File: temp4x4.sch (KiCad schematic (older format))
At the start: 15 parts, among them J1 NUCLEO_CN6_1-6, J2 NUCLEO_CN5_10-1, U1 LP5907MFX-3.3_NOPB, U2 ADS124S08IPBS

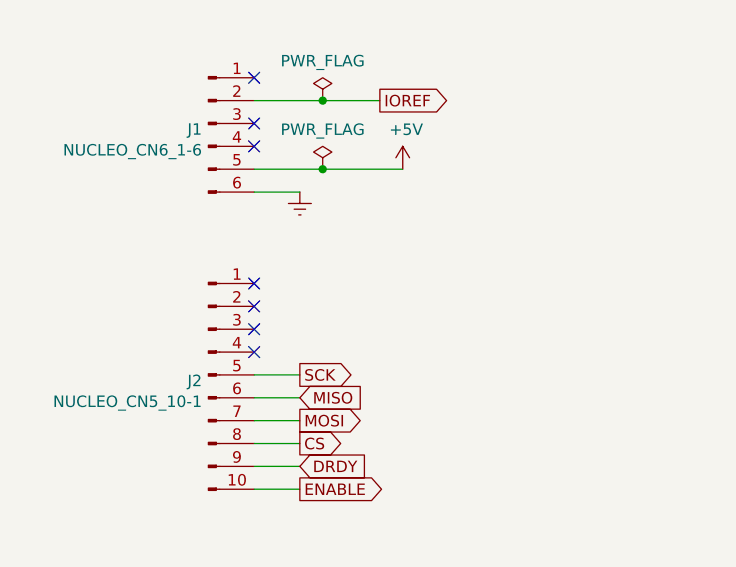
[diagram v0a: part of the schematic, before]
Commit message: added second GND connection through second pin header
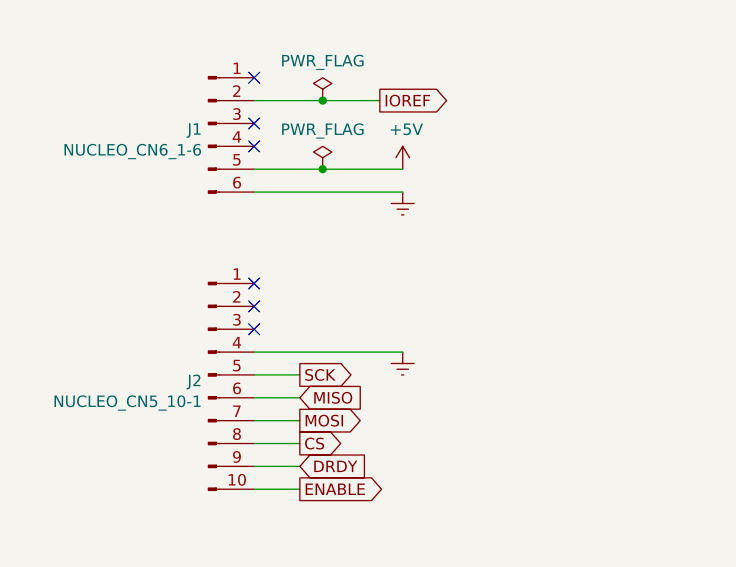
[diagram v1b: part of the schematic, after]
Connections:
- net Earth: now also J2.4 (Pin_4)
- no-connect marks 9 -> 8
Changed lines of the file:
@@
 L power:Earth #PWR03
 U 1 1 5ECDA4EC
-P 1750 3450
-F 0 "#PWR03" H 1750 3200 50  0001 C CNN
-F 1 "Earth" H 1750 3300 50  0001 C CNN
-F 2 "" H 1750 3450 50  0001 C CNN
-F 3 "~" H 1750 3450 50  0001 C CNN
-	1    1750 3450
-	1    0    0    -1
-$EndComp
-Wire Wire Line
-	1550 3450 1750 3450
+P 2200 3450
+F 0 "#PWR03" H 2200 3200 50  0001 C CNN
+F 1 "Earth" H 2200 3300 50  0001 C CNN
+F 2 "" H 2200 3450 50  0001 C CNN
+F 3 "~" H 2200 3450 50  0001 C CNN
+	1    2200 3450
+	1    0    0    -1
+$EndComp
+Wire Wire Line
+	1550 3450 2200 3450
 Wire Wire Line
 	1550 4250 1750 4250
@@
 	1    0    0    -1
 $EndComp
-NoConn ~ 1550 4150
 NoConn ~ 1550 4050
 NoConn ~ 1550 3950
@@
 Wire Wire Line
 	5800 3300 5800 4350
+$Comp
+L power:Earth #PWR?
+U 1 1 5EC59F0A
+P 2200 4150
+F 0 "#PWR?" H 2200 3900 50  0001 C CNN
+F 1 "Earth" H 2200 4000 50  0001 C CNN
+F 2 "" H 2200 4150 50  0001 C CNN
+F 3 "~" H 2200 4150 50  0001 C CNN
+	1    2200 4150
+	1    0    0    -1
+$EndComp
+Wire Wire Line
+	1550 4150 2200 4150
 $EndSCHEMATC

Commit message: completed ground connections
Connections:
- net Earth: no longer J2.4 (Pin_4)
- no-connect marks 8 -> 9
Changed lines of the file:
@@
 Wire Wire Line
 	5800 3300 5800 4350
-$Comp
-L power:Earth #PWR?
-U 1 1 5EC59F0A
-P 2200 4150
-F 0 "#PWR?" H 2200 3900 50  0001 C CNN
-F 1 "Earth" H 2200 4000 50  0001 C CNN
-F 2 "" H 2200 4150 50  0001 C CNN
-F 3 "~" H 2200 4150 50  0001 C CNN
-	1    2200 4150
-	1    0    0    -1
-$EndComp
-Wire Wire Line
-	1550 4150 2200 4150
+NoConn ~ 1550 4150
 $EndSCHEMATC

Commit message: start re-doing the analog part
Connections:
- net RTD_0_1/IEXC: no longer names the net of U2.2 (AIN5)
- net RTD_0_1/REF_N: no longer names the net of U2.29 (REFN0)
- net RTD_0_1/REF_P: no longer names the net of U2.30 (REFP0)
- net RTD_0_1/RTD0_N: no longer names the net of U2.20 (GPIO2_AIN10)
- net RTD_0_1/RTD0_P: no longer names the net of U2.19 (GPIO3_AIN11)
- net RTD_0_1/RTD1_N: no longer names the net of U2.22 (GPIO0_AIN8)
- net RTD_0_1/RTD1_P: no longer names the net of U2.21 (GPIO1_AIN9)
- net RTD_1_2/IEXC: no longer names the net of U2.7 (AIN0)
- net RTD_1_2/REF_N: no longer names the net of U2.31 (REFN1_AIN7)
- net RTD_1_2/REF_P: no longer names the net of U2.32 (REFP1_AIN6)
- net RTD_1_2/RTD0_N: no longer names the net of U2.4 (AIN3)
- net RTD_1_2/RTD0_P: no longer names the net of U2.3 (AIN4)
- net RTD_1_2/RTD1_N: no longer names the net of U2.6 (AIN1)
- net RTD_1_2/RTD1_P: no longer names the net of U2.5 (AIN2)
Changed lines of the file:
@@
 $Descr A4 11693 8268
 encoding utf-8
-Sheet 1 3
+Sheet 1 1
 Title ""
 Date ""
@@
 Text GLabel 6250 1800 2    50   Input ~ 0
 IOREF
-$Sheet
-S 3950 4050 1250 1150
-U 5EC374D6
-F0 "RTD_0_1" 50
-F1 "two_rtd_plus_ref.sch" 50
-F2 "IEXC" I R 5200 4250 50
-F3 "RTD0_P" O R 5200 4400 50
-F4 "RTD0_N" O R 5200 4500 50
-F5 "RTD1_P" O R 5200 4650 50
-F6 "RTD1_N" O R 5200 4750 50
-F7 "REF_P" O R 5200 4900 50
-F8 "REF_N" O R 5200 5000 50
-$EndSheet
 Wire Wire Line
 	6700 4950 6700 5000
@@
 Connection ~ 6700 4950
 NoConn ~ 7000 2650
-$Sheet
-S 3950 2350 1250 1150
-U 5ED0B429
-F0 "RTD_1_2" 50
-F1 "two_rtd_plus_ref.sch" 50
-F2 "IEXC" I R 5200 2550 50
-F3 "RTD0_P" O R 5200 2700 50
-F4 "RTD0_N" O R 5200 2800 50
-F5 "RTD1_P" O R 5200 2950 50
-F6 "RTD1_N" O R 5200 3050 50
-F7 "REF_P" O R 5200 3200 50
-F8 "REF_N" O R 5200 3300 50
-$EndSheet
 $Comp
 L power:Earth #PWR06
@@
 NoConn ~ 1550 3950
 NoConn ~ 1550 3850
-Wire Wire Line
-	5200 3200 5900 3200
-Wire Wire Line
-	5200 3300 5800 3300
-Wire Wire Line
-	5650 4250 5200 4250
-Wire Wire Line
-	6000 4400 5200 4400
-Wire Wire Line
-	6100 4500 5200 4500
-Wire Wire Line
-	6200 4650 5200 4650
-Wire Wire Line
-	6300 4750 5200 4750
-Wire Wire Line
-	6400 4900 5200 4900
-Wire Wire Line
-	6500 5000 5200 5000
-Wire Wire Line
-	6700 2550 6700 2850
-Wire Wire Line
-	6700 2850 7000 2850
-Wire Wire Line
-	5200 2550 6700 2550
-Wire Wire Line
-	5200 2700 6600 2700
-Wire Wire Line
-	5200 2800 6500 2800
-Wire Wire Line
-	7000 3350 5650 3350
-Wire Wire Line
-	5650 3350 5650 4250
 $Comp
 L ADS124S08IPBS:ADS124S08IPBS U2
@@
 	1    0    0    -1
 $EndComp
-Wire Wire Line
-	6600 3250 7000 3250
-Wire Wire Line
-	6600 2700 6600 3250
-Wire Wire Line
-	6500 3150 7000 3150
-Wire Wire Line
-	6500 2800 6500 3150
-Wire Wire Line
-	5200 2950 6000 2950
-Wire Wire Line
-	6400 3050 7000 3050
-Wire Wire Line
-	5200 3050 6300 3050
-Wire Wire Line
-	6300 3050 6300 2950
-Wire Wire Line
-	6300 2950 7000 2950
-Wire Wire Line
-	6000 2950 6000 3150
-Wire Wire Line
-	6000 3150 6400 3150
-Wire Wire Line
-	6400 3150 6400 3050
-Wire Wire Line
-	6200 3650 7000 3650
-Wire Wire Line
-	6200 3650 6200 4650
-Wire Wire Line
-	6300 4750 6300 3550
-Wire Wire Line
-	6300 3550 7000 3550
-Wire Wire Line
-	6000 4400 6000 3850
-Wire Wire Line
-	6000 3850 7000 3850
-Wire Wire Line
-	6100 4500 6100 3750
-Wire Wire Line
-	6100 3750 7000 3750
-Wire Wire Line
-	6400 4050 7000 4050
-Wire Wire Line
-	6400 4050 6400 4900
-Wire Wire Line
-	6500 4150 7000 4150
-Wire Wire Line
-	6500 4150 6500 5000
-Wire Wire Line
-	5900 4250 6850 4250
-Wire Wire Line
-	6850 4250 6850 4350
-Wire Wire Line
-	6850 4350 7000 4350
-Wire Wire Line
-	5900 3200 5900 4250
-Wire Wire Line
-	5800 4350 6750 4350
-Wire Wire Line
-	6750 4350 6750 4450
-Wire Wire Line
-	6750 4450 7000 4450
-Wire Wire Line
-	5800 3300 5800 4350
 NoConn ~ 1550 4150
 $EndSCHEMATC

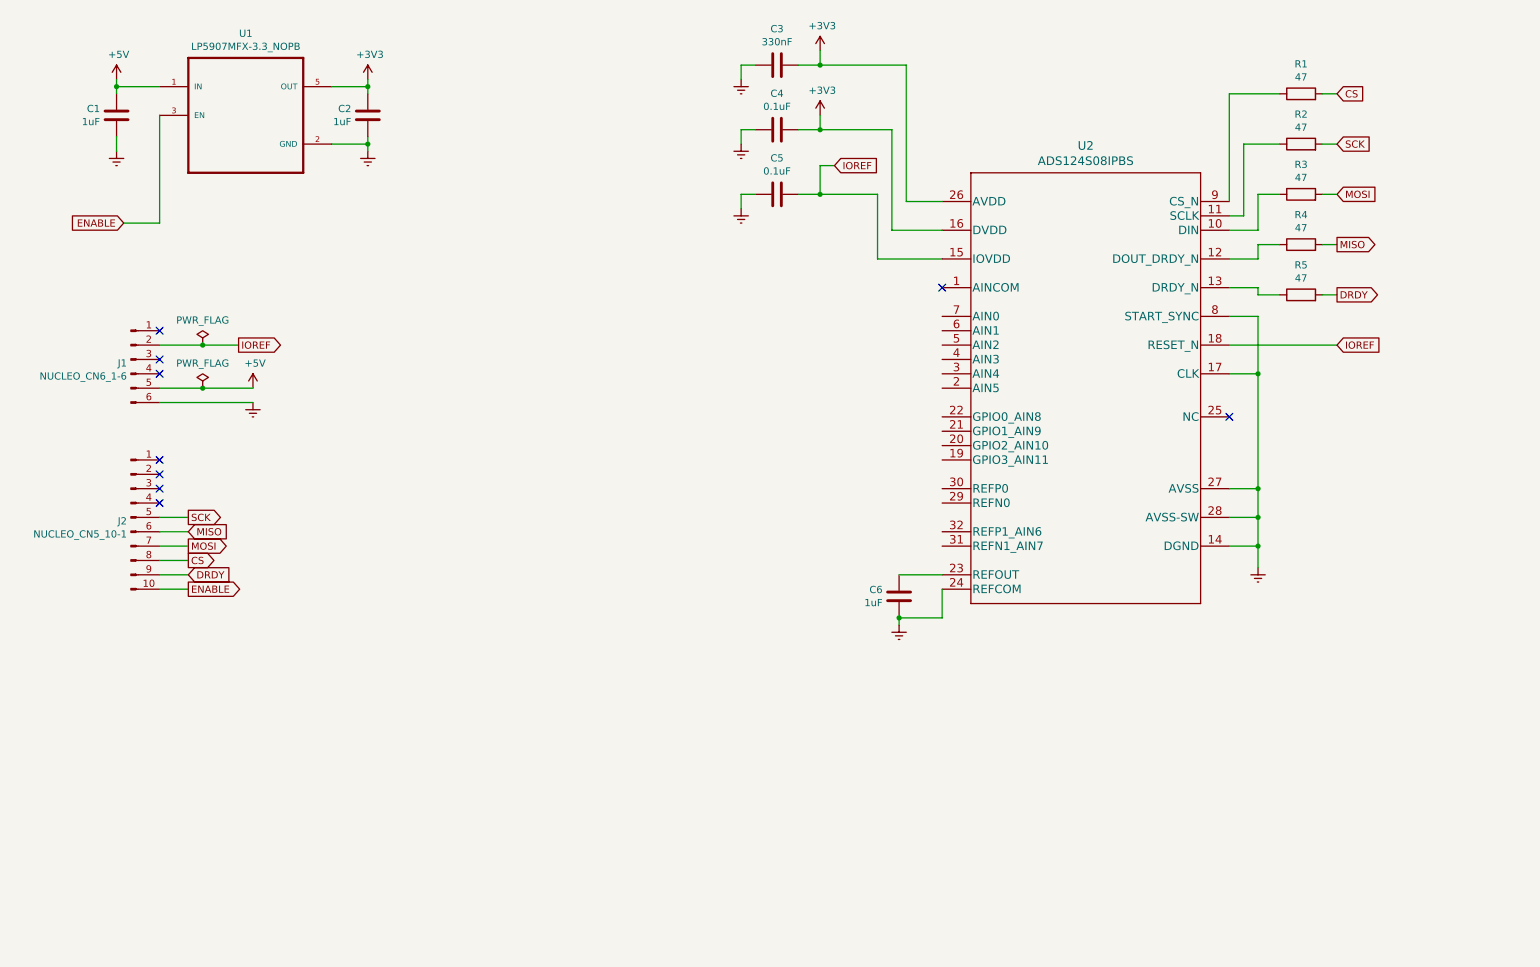
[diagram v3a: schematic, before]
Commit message: re-done analog part of the circuit
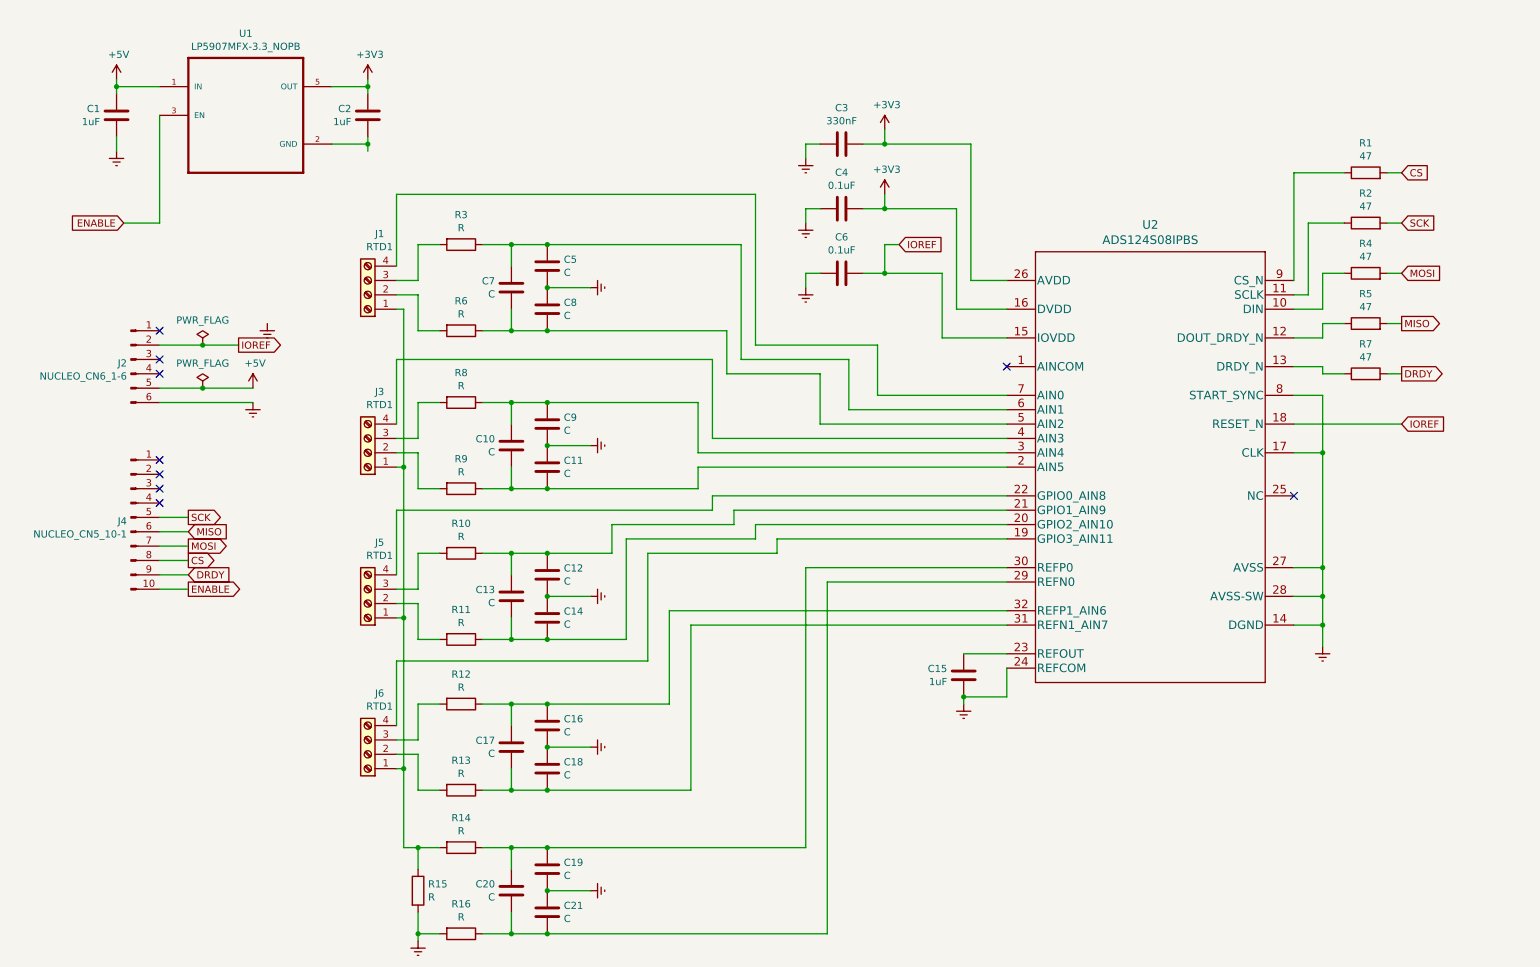
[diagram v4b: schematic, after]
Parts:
- added C10, C11, C12, C13, C14, C16, C17, C18, C19, C20, C21, C5, C7, C8, C9: C, Capacitor_SMD:C_0805_2012Metric_Pad1.15x1.40mm_HandSolder, symbol Device:C
- added J1, J3, J5, J6: RTD1, temp4x4:screw_term_4x, symbol Connector:Screw_Terminal_01x04
- added R10, R11, R12, R13, R14, R15, R16, R3, R6, R8, R9: R, Resistor_SMD:R_0805_2012Metric_Pad1.15x1.40mm_HandSolder, symbol Device:R
- renumbered C6 to C15, C5 to C6, J1 to J2, J2 to J4, R3 to R4, R4 to R5, R5 to R7
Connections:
- net Earth: now also C11.1, C12.2, C14.1, C16.2, C18.1, C19.2, C21.1, C5.2, C8.1, C9.2, R15.2, R16.2; no longer C2.2, U1.2 (GND)
- net at U2.19 (GPIO3_AIN11): now also J6.4 (Pin_4)
- net at U2.2 (AIN5): now also C10.1, C11.2, R9.1
- net at U2.20 (GPIO2_AIN10): now also C13.1, C14.2, R11.1
- net at U2.21 (GPIO1_AIN9): now also C12.1, C13.2, R10.1
- net at U2.22 (GPIO0_AIN8): now also J5.4 (Pin_4)
- net at U2.29 (REFN0): now also C20.1, C21.2, R16.1
- net at U2.3 (AIN4): now also C10.2, C9.1, R8.1
- net at U2.30 (REFP0): now also C19.1, C20.2, R14.1
- net at U2.31 (REFN1_AIN7): now also C17.1, C18.2, R13.1
- net at U2.32 (REFP1_AIN6): now also C16.1, C17.2, R12.1
- net at U2.4 (AIN3): now also J3.4 (Pin_4)
- net at U2.5 (AIN2): now also C7.1, C8.2, R6.1
- net at U2.6 (AIN1): now also C5.1, C7.2, R3.1
- net at U2.7 (AIN0): now also J1.4 (Pin_4)
- new net: C2.2, U1.2 (GND)
- new net: J1.1 (Pin_1), J3.1 (Pin_1), J5.1 (Pin_1), J6.1 (Pin_1), R14.2, R15.1
- new net: J1.2 (Pin_2), R6.2
- new net: J1.3 (Pin_3), R3.2
- new net: J3.2 (Pin_2), R9.2
- new net: J3.3 (Pin_3), R8.2
- new net: J6.2 (Pin_2), R13.2
- new net: J6.3 (Pin_3), R12.2
- new net: J5.2 (Pin_2), R11.2
- new net: J5.3 (Pin_3), R10.2
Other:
- moved on the sheet: C15, C3, C4, C6, R1, R2, R4, R5, R7, U2

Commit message: re-done layout
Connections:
- net Earth: now also C2.2, U1.2 (GND)
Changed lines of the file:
@@
 Wire Wire Line
 	4250 7150 6200 7150
+$Comp
+L power:Earth #PWR?
+U 1 1 5F22F3E7
+P 3000 1700
+F 0 "#PWR?" H 3000 1450 50  0001 C CNN
+F 1 "Earth" H 3000 1550 50  0001 C CNN
+F 2 "" H 3000 1700 50  0001 C CNN
+F 3 "~" H 3000 1700 50  0001 C CNN
+	1    3000 1700
+	1    0    0    -1
+$EndComp
 $EndSCHEMATC

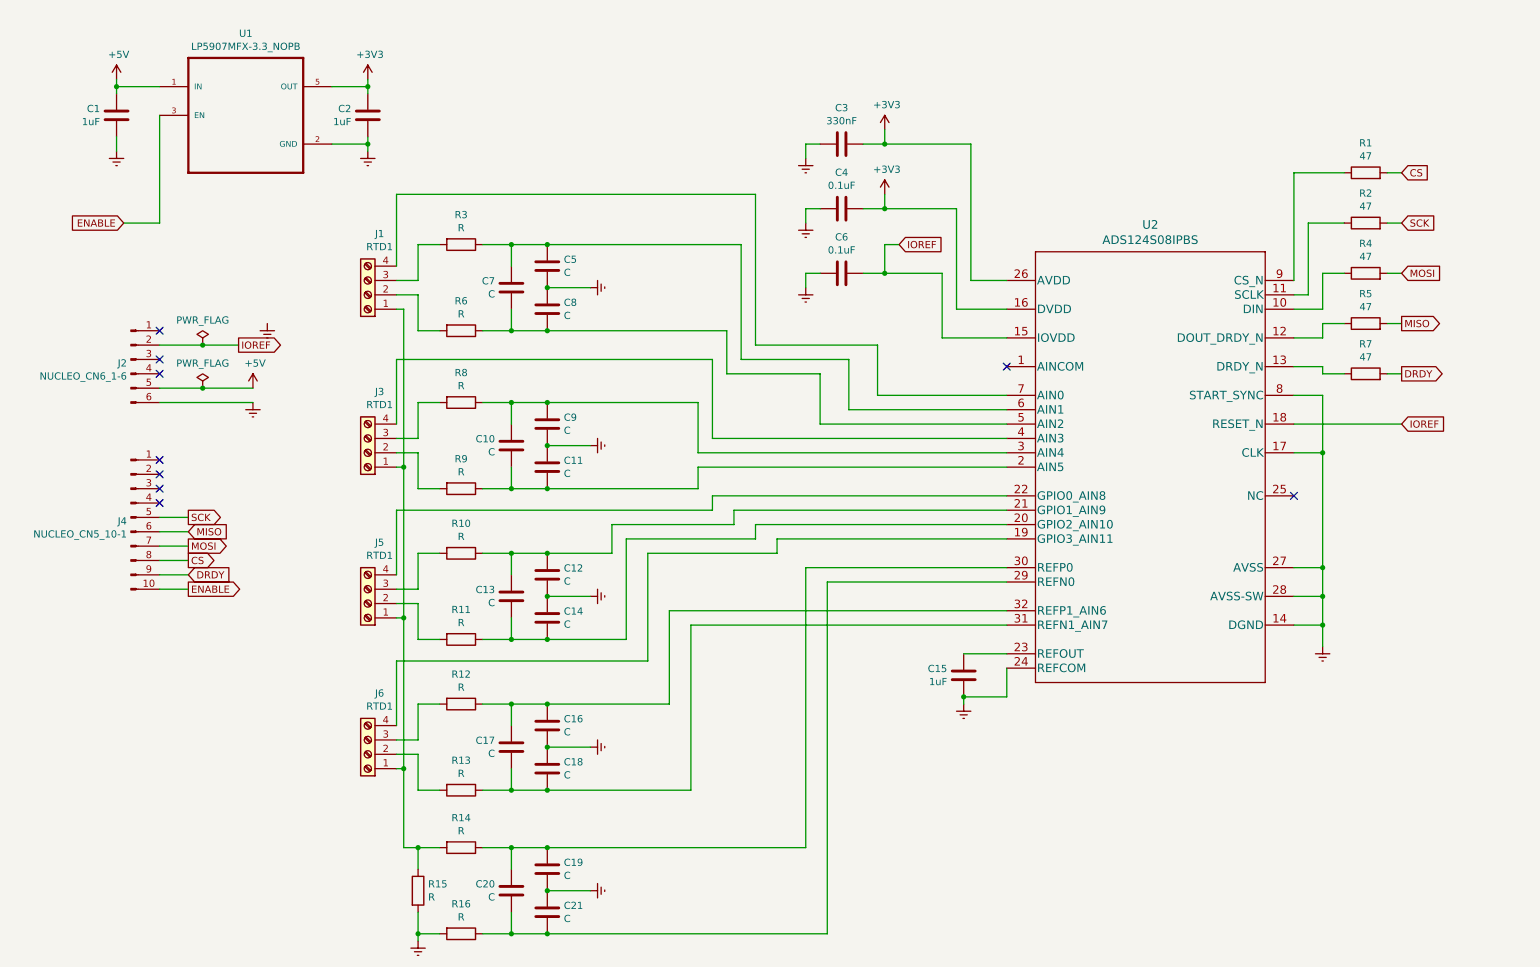
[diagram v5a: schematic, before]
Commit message: added silkscreen labels
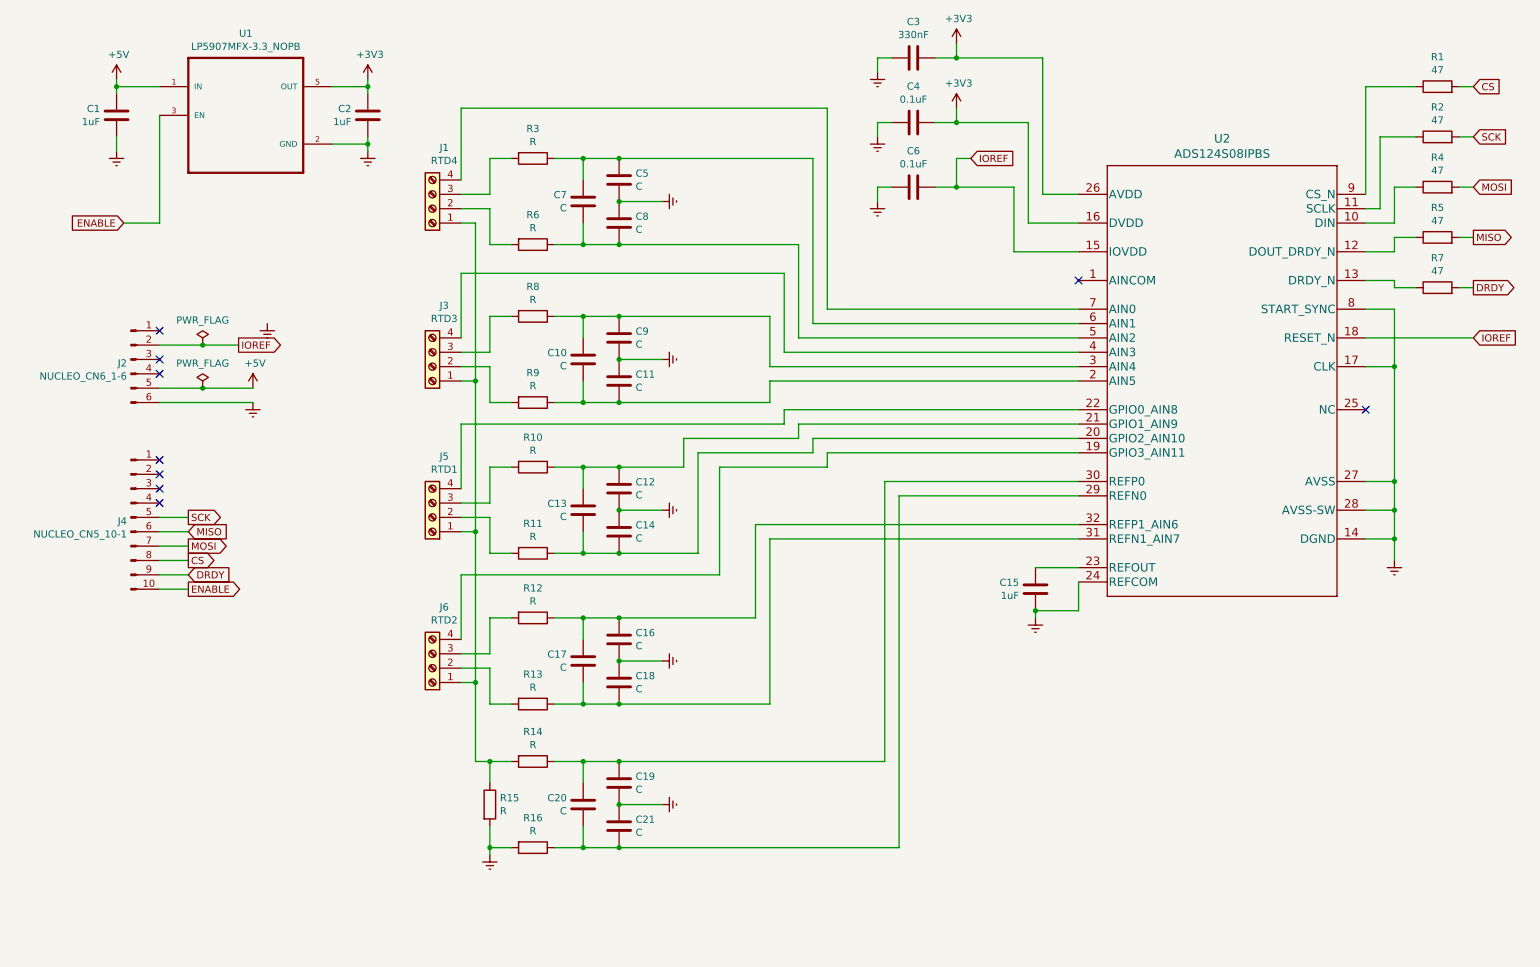
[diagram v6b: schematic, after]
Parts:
- J1: value RTD1 -> RTD4
- J3: value RTD1 -> RTD3
- J6: value RTD1 -> RTD2
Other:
- moved on the sheet: C10, C11, C12, C13, C14, C15, C16, C17, C18, C19, C20, C21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
